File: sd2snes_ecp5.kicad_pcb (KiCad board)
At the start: 4 copper layers, 101.8 x 83 mm, 184 parts, among them J201 SNESCART_EXT, J301 USB-C, J302 MicroSD, J501 FPGA_JTAG, P301 RESET, P302 FREEZE, P303 CPU_DEBUG, Q201 MMBT2222A, Q401 IRLML6402PbF, Q601 MMBT2222A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

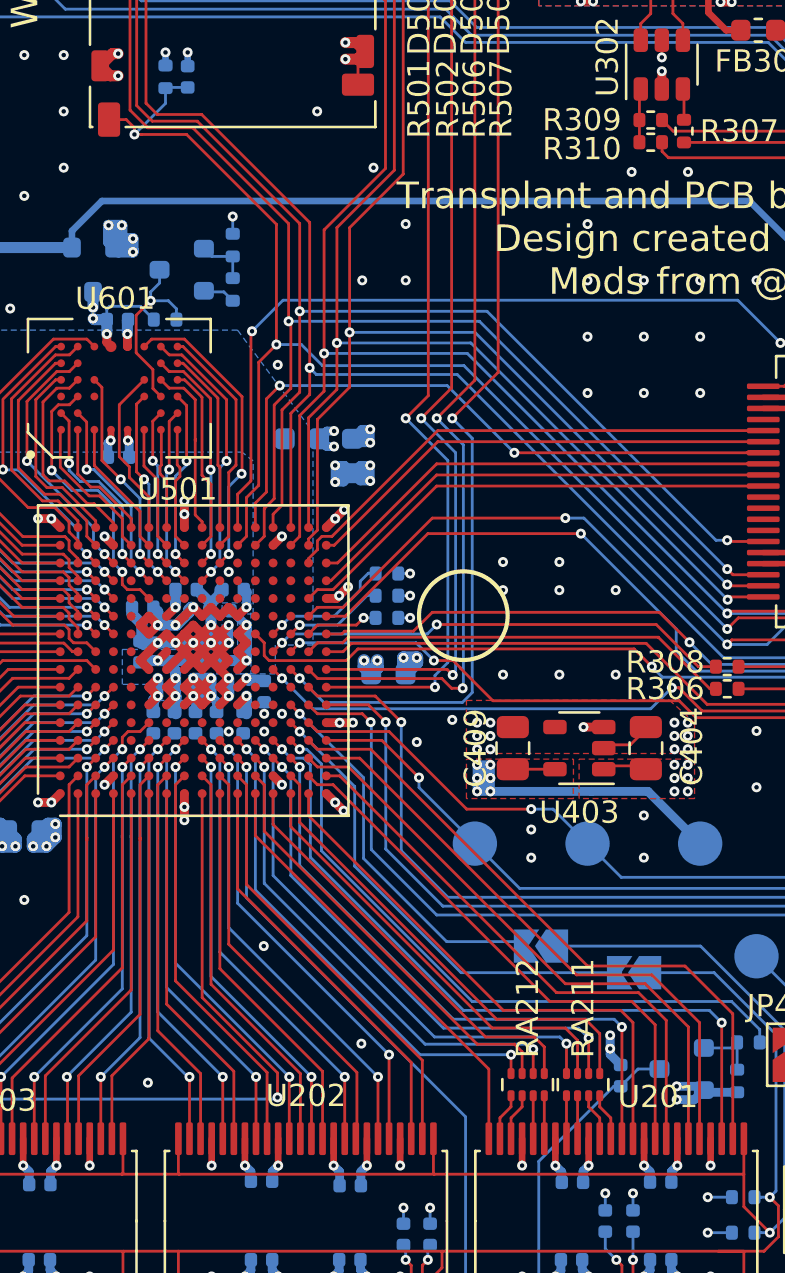
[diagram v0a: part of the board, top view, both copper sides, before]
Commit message: Fix labels on snes slot lines.
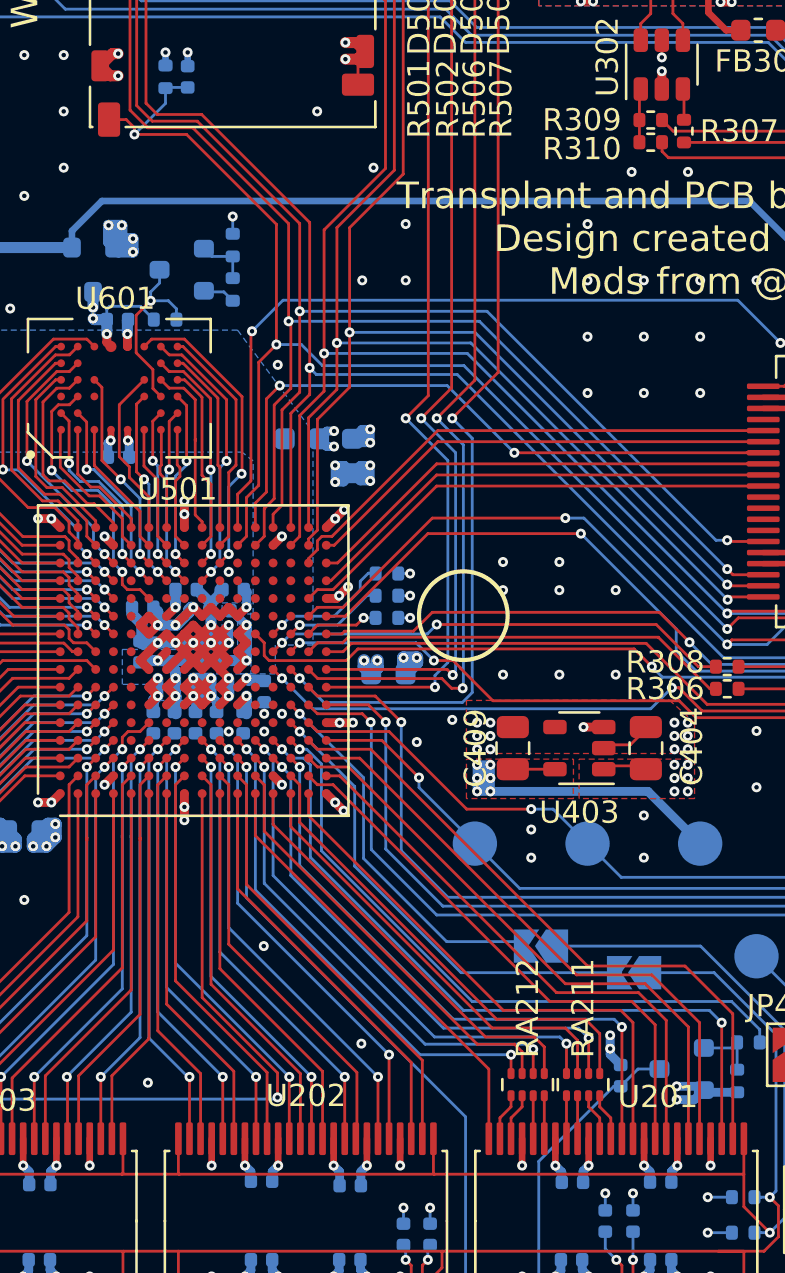
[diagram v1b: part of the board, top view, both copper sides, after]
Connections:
- U202 pad 26: ~SNES_ROMSEL_IN -> SNES_CPU_CLK_IN
- U202 pad 27: SNES_CPU_CLK_IN -> ~SNES_ROMSEL_IN
- U501 pad L1: SNES_CPU_CLK_IN -> ~SNES_ROMSEL_IN
- U501 pad L2: ~SNES_ROMSEL_IN -> SNES_CPU_CLK_IN
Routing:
- net ~SNES_ROMSEL_IN: track 19.8 -> 18.8 mm
- net SNES_CPU_CLK_IN: track 18.8 -> 19.8 mm
